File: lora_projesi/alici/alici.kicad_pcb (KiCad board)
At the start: 4 copper layers, 88 x 102 mm, 127 parts, among them J1 USB-C, J2 SMA, J3 RJ45, J4 u.FL (ANA ANTEN), J5 12 V GIRIS, J6 LAMBA, J7 MICRO-SIM, J8 u.FL (YARDIMCI ANTEN, ISTEGE 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, K1 SRD-12VDC-SL-A, Q1 AO3401A, Q2 MMBT2222A, Q3 MMBT2222A, Q4 MMBT2222A, SW1 DUGME, U1 ESP32-S3-WROOM-1-N4, U10 SIM7600SA, U11 AP2112K-3.3, U12 ESDA6V1-5SC6, U4 RFM95W-915S2, U5 TPS62933DRLR, U6 TPS62933DRLR, U7 USBLC6-2SC6, U8 TXB0104PW, U9 W5500, Y1 25 MHz

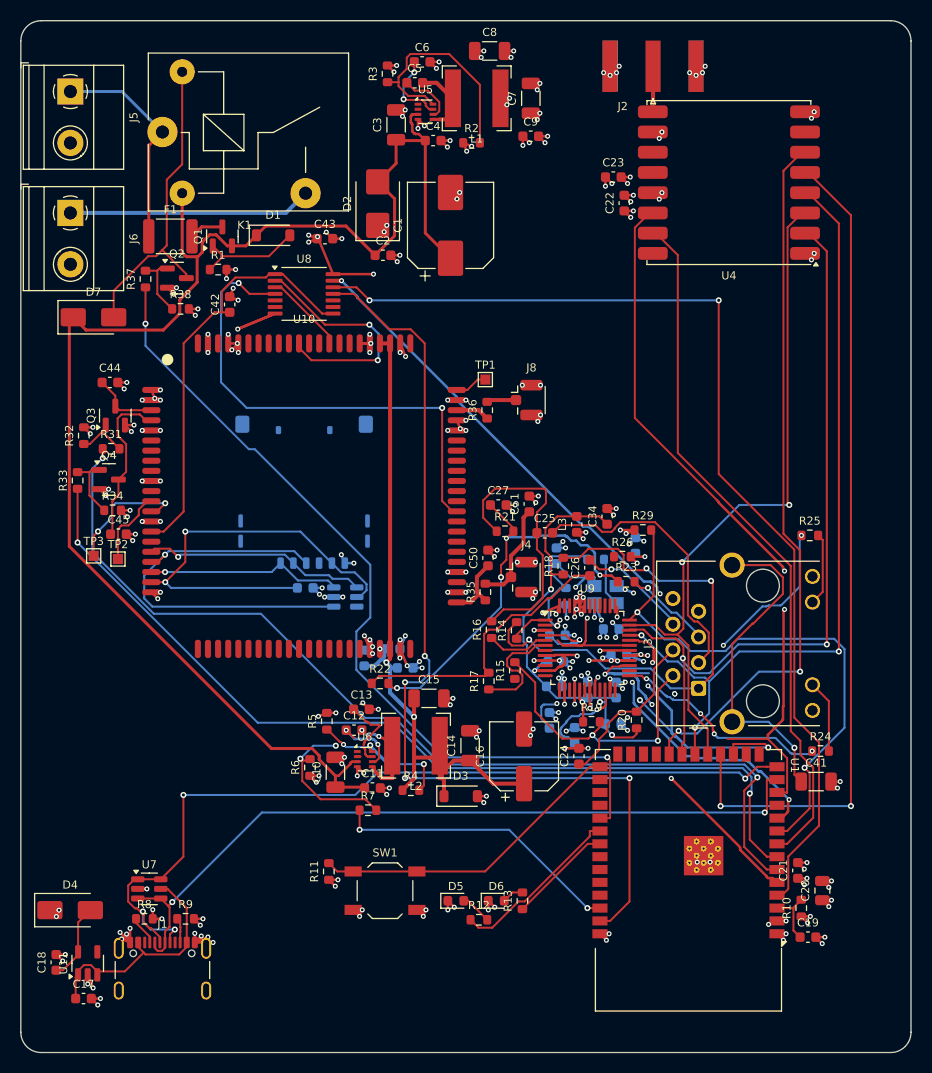
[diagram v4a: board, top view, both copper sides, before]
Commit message: Alici: XI/XO/ETH_CS icin dog-bone fan-out denemesi (ara hal)
Co-Authored-By: Claude Sonnet 5.5 <noreply@anthropic.com>
Claude-Session: https://claude.ai/code/session_01Q71gHQtKJ86ZE2CtYTYSwP
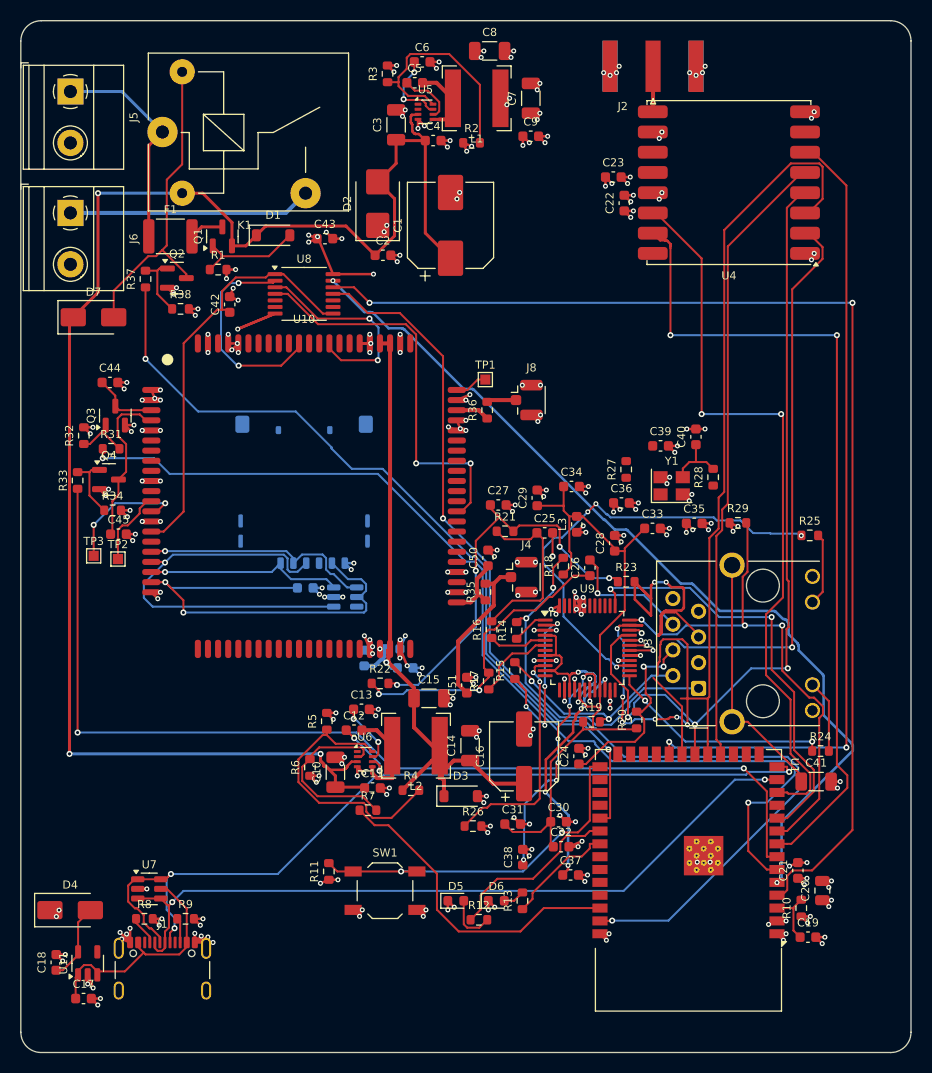
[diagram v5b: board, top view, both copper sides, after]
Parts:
- C28, C29, C30, C31, C32, C33, C35, C36, C37, C38, C39, C40, R27, R28, Y1: moved to F.Cu
- moved R26 30.5 mm to (44.7, 79.6)
- moved C33 19.7 mm to (62.4, 50.2)
- moved C51 19.0 mm to (44.1, 65.7)
- moved C32 16.4 mm to (53.4, 81.7), turned to 0 degrees
- moved C29 16.3 mm to (51.0, 47.2), turned to 90 degrees
- moved C31 15.2 mm to (48.6, 79.4), turned to 0 degrees
- moved C39 15.0 mm to (63.2, 42.0), turned to 0 degrees
- moved C35 14.9 mm to (66.6, 49.7)
- moved R28 14.2 mm to (68.4, 45.1), turned to 90 degrees
- moved R27 13.9 mm to (59.8, 44.4)
- moved C37 13.8 mm to (54.3, 84.4), turned to 0 degrees
- moved C38 13.8 mm to (49.6, 82.7)
- moved C30 13.4 mm to (53.2, 79.2)
- moved Y1 12.6 mm to (64.3, 46.0)
- moved C36 12.5 mm to (59.4, 47.7)
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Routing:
- net SPI_MOSI: track 68.4 -> 108.1 mm, vias 2 -> 6
- net ETH_CS: track 35.0 -> 1.14 mm, vias 4 -> 1
- net XO: track 34.8 -> 1.74 mm, vias 3 -> 1
- net RCT: track 8.80 -> 40.3 mm, vias 1 -> 2
- net RD_P: track 27.9 -> 2.56 mm, vias 0 -> 1
- net EXRES1: track 0.00 -> 23.0 mm, vias 0 -> 2
- net +3V3A: track 65.6 -> 88.5 mm, vias 9 -> 2
- net LORA_NSS: track 82.7 -> 61.5 mm, vias 2 -> 0
- net W_TXP: track 0.00 -> 17.8 mm, vias 0 -> 4
- net XI: track 19.7 -> 2.34 mm, vias 3 -> 1
- net TD_P: track 52.0 -> 35.5 mm, vias 3 -> 2
- net 1V2O: track 9.43 -> 24.2 mm, vias 1 -> 4
- net TOCAP: track 10.8 -> 24.3 mm, vias 2 -> 6
- net +12V: track 145.9 -> 158.9 mm, vias 0 -> 3
- net LORA_DIO1: track 69.2 -> 82.1 mm, vias 0 -> 2
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
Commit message: Alici: fan-out sonrasi yeniden yonlendirme (ara hal)
Co-Authored-By: Claude Sonnet 5.5 <noreply@anthropic.com>
Claude-Session: https://claude.ai/code/session_01Q71gHQtKJ86ZE2CtYTYSwP
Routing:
- net XI: track 2.34 -> 6.42 mm
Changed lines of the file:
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@@
   (segment (start 66.0895 43.6271) (end 66.7384 43.6271) (width 0.2) (layer "F.Cu") (net 90))
   (segment (start 67.7648 43.6271) (end 68.4405 44.3028) (width 0.2) (layer "F.Cu") (net 90))
+  (segment (start 60.2 45.5) (end 61 46.3) (width 0.25) (layer "F.Cu") (net 91))
+  (segment (start 61 46.3) (end 62.7 46.3) (width 0.25) (layer "F.Cu") (net 91))
+  (segment (start 60.15 45.5) (end 60.2 45.5) (width 0.25) (layer "F.Cu") (net 91))
   (segment (start 60.1625 62.25) (end 62.5 62.25) (width 0.2) (layer "F.Cu") (net 91))
+  (segment (start 59.8426 45.1841) (end 60.15 45.5) (width 0.25) (layer "F.Cu") (net 91))
+  (segment (start 62.7 46.3) (end 63.2405 46.8278) (width 0.25) (layer "F.Cu") (net 91))
   (via (at 62.5 62.25) (size 0.5) (drill 0.25) (layers "F.Cu" "B.Cu") (net 91))
   (segment (start 60.1625 61.75) (end 61.9 61.75) (width 0.2) (layer "F.Cu") (net 92))

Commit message: Alici: RD_P/SPI_MISO yeniden yonlendirme (ara hal)
Co-Authored-By: Claude Sonnet 5.5 <noreply@anthropic.com>
Claude-Session: https://claude.ai/code/session_01Q71gHQtKJ86ZE2CtYTYSwP
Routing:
- net SPI_MISO: track 64.8 -> 0.00 mm, vias 2 -> 0
- net XO: track 1.74 -> 32.0 mm, vias 1 -> 5
- net XI: track 6.42 -> 27.6 mm
- net ETH_CS: track 1.14 -> 22.1 mm, vias 1 -> 3
- net RD_P: track 2.56 -> 0.00 mm, vias 1 -> 0

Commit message: Alici: 0 baglantisiz, 0 DRC hatasi; sema/xml TXB0104 A4/B4 toprak duzeltmesi
Co-Authored-By: Claude Sonnet 5.5 <noreply@anthropic.com>
Claude-Session: https://claude.ai/code/session_01Q71gHQtKJ86ZE2CtYTYSwP
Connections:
- U8 pad 10: (no net) -> GND
- U8 pad 5: (no net) -> GND
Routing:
- net SPI_MISO: track 0.00 -> 63.7 mm, vias 0 -> 4
- net RD_P: track 0.00 -> 24.1 mm, vias 0 -> 1
- net GND: track 228.9 -> 232.1 mm, vias 233 -> 232
- net XO: vias 5 -> 4
- net XI: vias 1 -> 0
- net ETH_CS: vias 3 -> 2
